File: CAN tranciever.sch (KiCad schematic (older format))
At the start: 0 parts

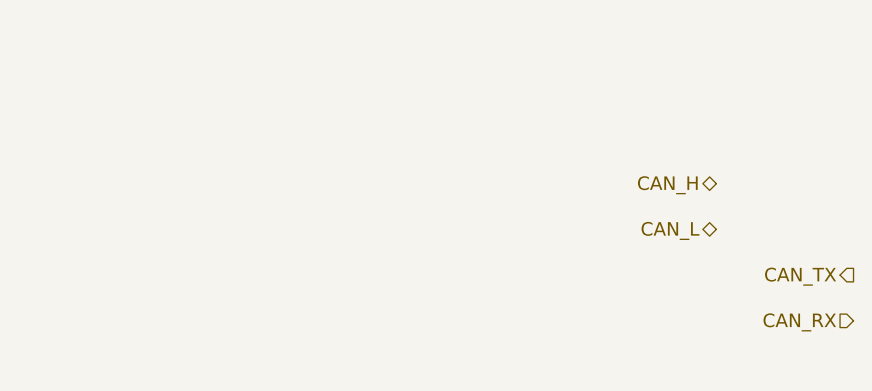
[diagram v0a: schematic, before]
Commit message: Imported CAN and PSU blocks from infrastructure rep
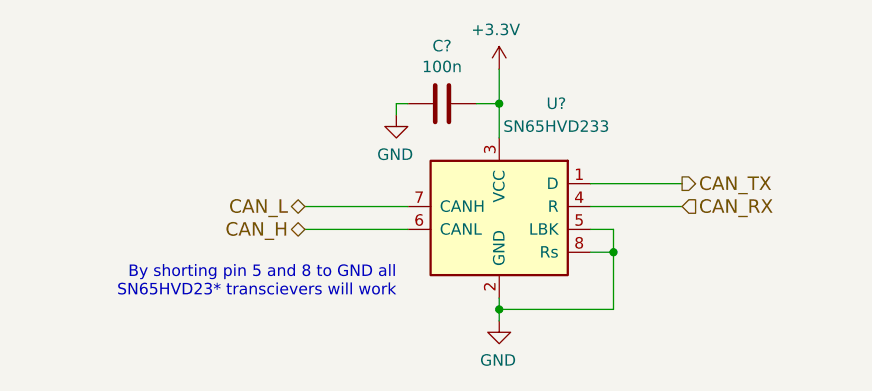
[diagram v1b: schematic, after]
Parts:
- added C?: 100n, symbol Device:C
- added U?: SN65HVD233, Package_SO:SOIC-8_3.9x4.9mm_P1.27mm, symbol Interface_CAN_LIN:SN65HVD233
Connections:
- net CAN_H: now also U?.6 (CANL)
- net CAN_L: now also U?.7 (CANH)
- net CAN_RX: now also U?.4 (R)
- net CAN_TX: now also U?.1 (D)
- new net +3V3: C?.2, U?.3 (VCC)
- new net GND: C?.1, U?.2 (GND), U?.5 (LBK), U?.8 (Rs)
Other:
- note added: "By shorting pin 5 and 8 to GND all\nSN65HVD23* transcievers will work"
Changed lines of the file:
@@
 EESchema Schematic File Version 4
+LIBS:TU-cache
 EELAYER 30 0
 EELAYER END
 $Descr A4 11693 8268
 encoding utf-8
-Sheet 5 6
+Sheet 4 6
 Title ""
 Date ""
@@
 Comment4 ""
 $EndDescr
-Text HLabel 6900 3100 0    59   BiDi ~ 0
+Text HLabel 5100 3300 0    59   BiDi ~ 0
 CAN_H
-Text HLabel 6900 3300 0    59   BiDi ~ 0
+Text HLabel 5100 3200 0    59   BiDi ~ 0
 CAN_L
-Text HLabel 7500 3500 0    59   Output ~ 0
+Text HLabel 6750 3100 2    59   Output ~ 0
 CAN_TX
-Text HLabel 7500 3700 0    59   Input ~ 0
+Text HLabel 6750 3200 2    59   Input ~ 0
 CAN_RX
+Wire Wire Line
+	6750 3100 6350 3100
+Wire Wire Line
+	6350 3200 6750 3200
+Wire Wire Line
+	5550 3200 5100 3200
+Wire Wire Line
+	5100 3300 5550 3300
+Wire Wire Line
+	5950 2900 5950 2750
+$Comp
+L power:+3.3V #PWR?
+U 1 1 5EEB36C2
+P 5950 2600
+F 0 "#PWR?" H 5950 2450 50  0001 C CNN
+F 1 "+3.3V" H 5965 2773 50  0000 C CNN
+F 2 "" H 5950 2600 50  0001 C CNN
+F 3 "" H 5950 2600 50  0001 C CNN
+	1    5950 2600
+	-1   0    0    -1
+$EndComp
+$Comp
+L power:GND #PWR?
+U 1 1 5EEB3802
+P 5950 3700
+F 0 "#PWR?" H 5950 3450 50  0001 C CNN
+F 1 "GND" H 5955 3527 50  0000 C CNN
+F 2 "" H 5950 3700 50  0001 C CNN
+F 3 "" H 5950 3700 50  0001 C CNN
+	1    5950 3700
+	-1   0    0    -1
+$EndComp
+Wire Wire Line
+	5950 3700 5950 3650
+$Comp
+L Device:C C?
+U 1 1 5EEB3AF7
+P 5700 2750
+F 0 "C?" V 5448 2750 50  0000 C CNN
+F 1 "100n" V 5539 2750 50  0000 C CNN
+F 2 "" H 5738 2600 50  0001 C CNN
+F 3 "~" H 5700 2750 50  0001 C CNN
+	1    5700 2750
+	0    -1   1    0
+$EndComp
+Wire Wire Line
+	5850 2750 5950 2750
+Connection ~ 5950 2750
+Wire Wire Line
+	5950 2750 5950 2600
+$Comp
+L power:GND #PWR?
+U 1 1 5EEB4720
+P 5500 2800
+F 0 "#PWR?" H 5500 2550 50  0001 C CNN
+F 1 "GND" H 5505 2627 50  0000 C CNN
+F 2 "" H 5500 2800 50  0001 C CNN
+F 3 "" H 5500 2800 50  0001 C CNN
+	1    5500 2800
+	-1   0    0    -1
+$EndComp
+Wire Wire Line
+	5500 2800 5500 2750
+Wire Wire Line
+	5500 2750 5550 2750
+$Comp
+L Interface_CAN_LIN:SN65HVD233 U?
+U 1 1 5FAEC37C
+P 5950 3200
+F 0 "U?" H 5700 3650 50  0000 C CNN
+F 1 "SN65HVD233" H 5700 3550 50  0000 C CNN
+F 2 "Package_SO:SOIC-8_3.9x4.9mm_P1.27mm" H 5950 2700 50  0001 C CNN
+F 3 "http://www.ti.com/lit/ds/symlink/sn65hvd234.pdf" H 5850 3600 50  0001 C CNN
+	1    5950 3200
+	-1   0    0    -1
+$EndComp
+Wire Wire Line
+	6350 3400 6450 3400
+Wire Wire Line
+	6450 3650 5950 3650
+Wire Wire Line
+	6450 3400 6450 3650
+Connection ~ 5950 3650
+Wire Wire Line
+	5950 3650 5950 3600
+Wire Wire Line
+	6350 3300 6450 3300
+Wire Wire Line
+	6450 3300 6450 3400
+Connection ~ 6450 3400
+Text Notes 5500 3600 2    50   ~ 0
+By shorting pin 5 and 8 to GND all\nSN65HVD23* transcievers will work
 $EndSCHEMATC
